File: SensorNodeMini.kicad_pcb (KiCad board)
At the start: 2 copper layers, 2 parts, among them U1 ArduinoProMini, U2 NRF24L01+

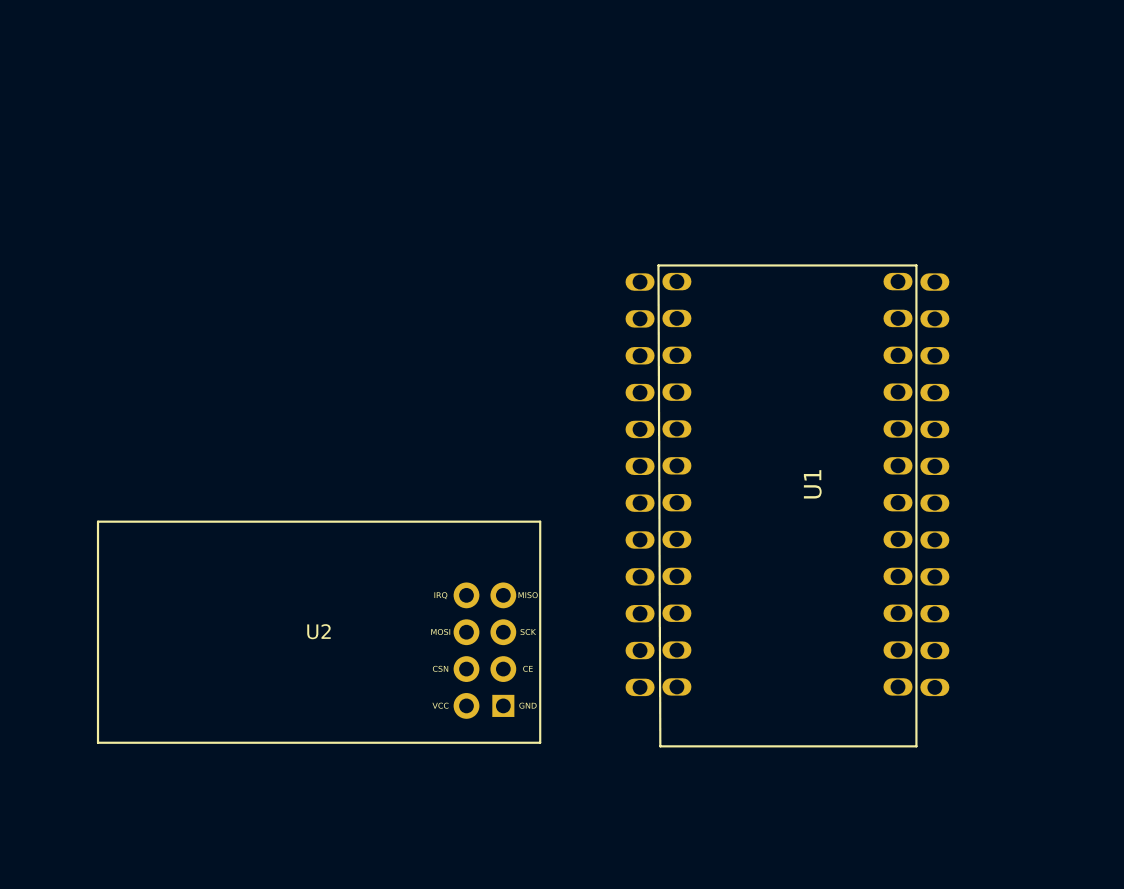
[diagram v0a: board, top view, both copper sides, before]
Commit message: added 3 mosfets, battery and connectors.
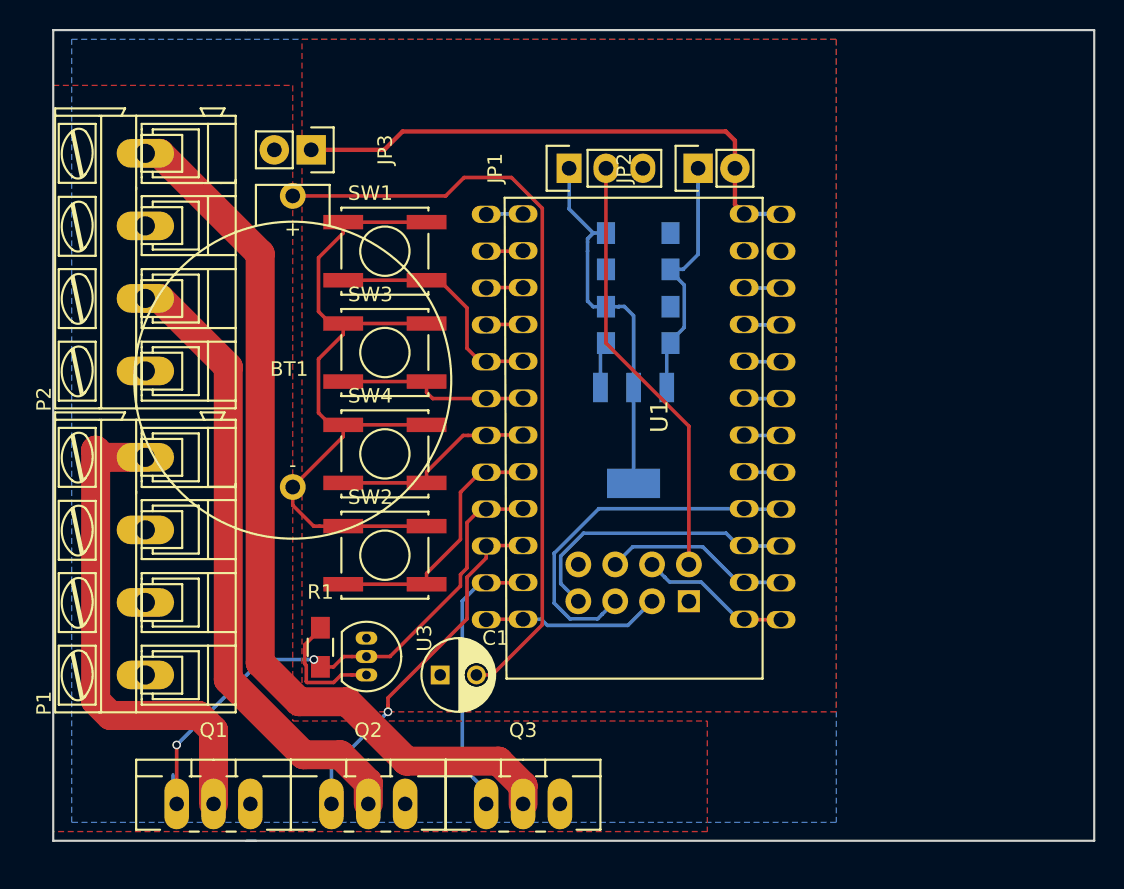
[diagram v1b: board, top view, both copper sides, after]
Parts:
- added BT1: Battery, MySensors:CR3032Holder, F.Cu at (139.1, 90.2)
- added C1: CP, Capacitors_ThroughHole:C_Radial_D5_L6_P2.5, F.Cu at (149.2, 110.5)
- added C2: 10u, Capacitors_SMD:C_0805_HandSoldering, B.Cu at (160.7, 86.4)
- added C3: 0.1u, Capacitors_SMD:C_0805_HandSoldering, B.Cu at (160.7, 81.3)
- added C4: 0.1u, Capacitors_SMD:C_0805_HandSoldering, B.Cu at (165.1, 86.4)
- added C5: 10u, Capacitors_SMD:C_0805_HandSoldering, B.Cu at (165.1, 81.3)
- added IC1: AMS1117, MySensors:SOT-223, B.Cu at (162.6, 94.0)
- added JP1: JUMPER3, Pin_Headers:Pin_Header_Straight_1x03, F.Cu at (158.1, 75.6)
- added JP2: JUMPER, Pin_Headers:Pin_Header_Straight_1x02, F.Cu at (167.0, 75.6)
- added JP3: JUMPER, Pin_Headers:Pin_Header_Straight_1x02, F.Cu at (140.3, 74.3)
- added P1: CONN_01X04, Connect:AK300-4, F.Cu at (128.9, 110.5)
- added P2: CONN_01X04, Connect:AK300-4, F.Cu at (128.9, 89.5)
- added Q1: Q_NMOS_GDS, TO_SOT_Packages_THT:TO-220_Neutral123_Vertical_LargePads, F.Cu at (133.6, 119.4)
- added Q2: Q_NMOS_GDS, TO_SOT_Packages_THT:TO-220_Neutral123_Vertical_LargePads, F.Cu at (144.3, 119.4)
- added Q3: Q_NMOS_GDS, TO_SOT_Packages_THT:TO-220_Neutral123_Vertical_LargePads, F.Cu at (154.9, 119.4)
- added R1: R, Resistors_SMD:R_0805_HandSoldering, F.Cu at (141.0, 108.6)
- added SW1: SW_PUSH, Buttons_Switches_SMD:SW_SPST_EVPBF, F.Cu at (145.4, 81.3)
- added SW2: SW_PUSH, Buttons_Switches_SMD:SW_SPST_EVPBF, F.Cu at (145.4, 102.2)
- added SW3: SW_PUSH, Buttons_Switches_SMD:SW_SPST_EVPBF, F.Cu at (145.4, 88.3)
- added SW4: SW_PUSH, Buttons_Switches_SMD:SW_SPST_EVPBF, F.Cu at (145.4, 95.2)
- added U3: DS18B20, TO_SOT_Packages_THT:TO-92_Inline_Narrow_Oval, F.Cu at (144.1, 108.0)
- U2: moved to B.Cu
- moved U1 11.6 mm to (162.6, 96.5)
- moved U2 11.3 mm to (158.8, 100.3), turned to 270 degrees
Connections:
- U1 pad 10: Net-(U1-Pad10) -> D7
- U1 pad 11: Net-(U1-Pad11) -> D8
- U1 pad 24: Net-(U1-Pad24) -> RAW
- U1 pad 9: Net-(U1-Pad9) -> D6
- U2 pad 8: VCC -> VCC_NRF
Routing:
- net VCC: track 0.00 -> 64.5 mm
- net Net-(P2-Pad4): track 0.00 -> 62.8 mm
- net GND: track 0.00 -> 55.2 mm
- net Net-(P2-Pad2): track 0.00 -> 44.2 mm
- net D6: track 0.00 -> 39.7 mm, vias 0 -> 2
- net RAW: track 0.00 -> 37.9 mm
- net Net-(P1-Pad4): track 0.00 -> 35.0 mm
- net VCC_NRF: track 0.00 -> 29.7 mm
- net Vout: track 0.00 -> 26.0 mm
- net SCK: track 0.00 -> 25.5 mm
- net D7: track 0.00 -> 24.8 mm, vias 0 -> 1
- net MISO: track 0.00 -> 19.8 mm
- net D8: track 0.00 -> 19.4 mm
- net Net-(SW2-Pad2): track 0.00 -> 18.0 mm
- net Net-(C4-Pad2): track 0.00 -> 17.3 mm
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- added copper zone on F.Cu, net +12V
- added copper zone on B.Cu, net GND
- added copper zone on F.Cu, net VCC
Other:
- board outline added: 71.8 x 55.9 mm
- net class +12v added: clearance 0.2, trace_width 2, via_dia 0.6, via_drill 0.4
- net class RAW added: clearance 0.2, trace_width 0.3, via_dia 0.6, via_drill 0.4

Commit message: routed everything, made gerbers.
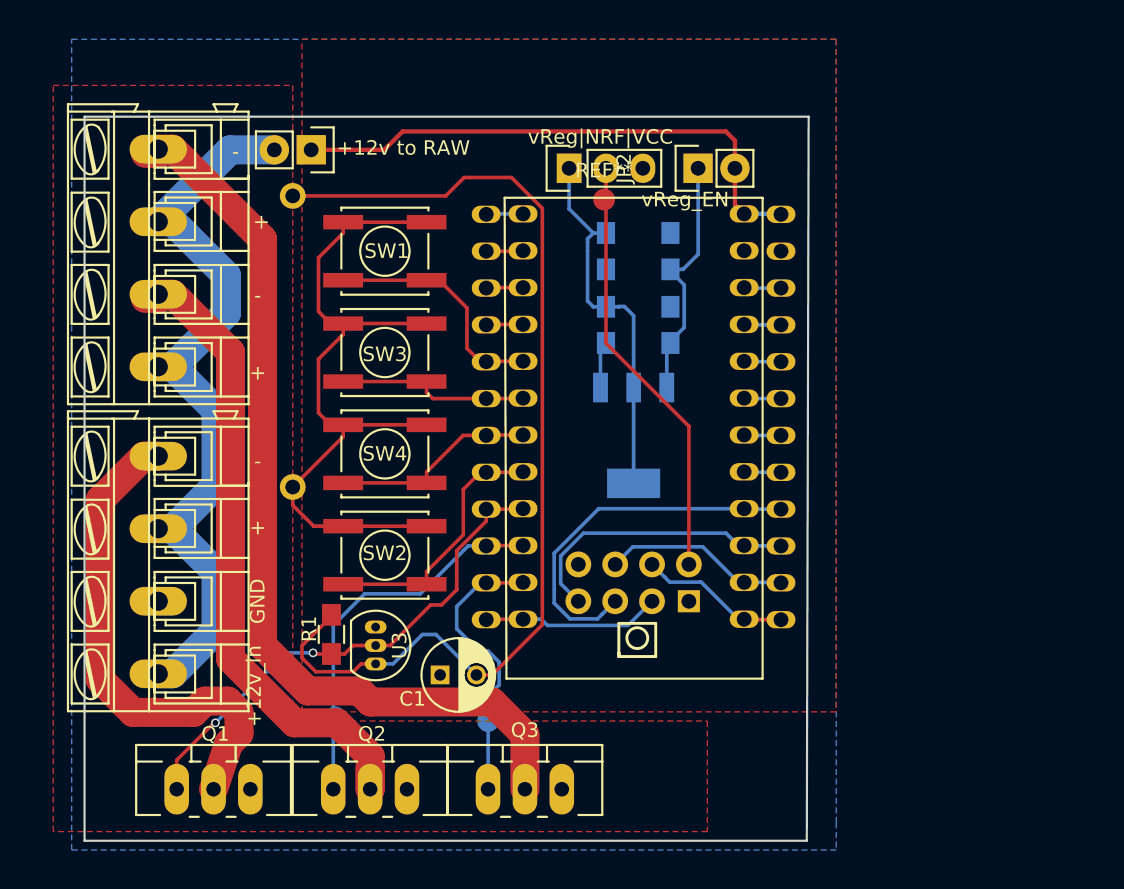
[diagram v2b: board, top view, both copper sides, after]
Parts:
- added REF**: Measurement_Point_Round-SMD-Pad_Small, Measurement_Points:Measurement_Point_Round-SMD-Pad_Small, F.Cu at (160.5, 77.7)
- added TP1: Measurement_Point_Round-SMD-Pad_Small, Measurement_Points:Measurement_Point_Round-SMD-Pad_Small, B.Cu at (137.8, 109.7)
- added TP2: Measurement_Point_Round-SMD-Pad_Small, Measurement_Points:Measurement_Point_Round-SMD-Pad_Small, B.Cu at (142.0, 113.4)
- added TP3: Measurement_Point_Round-SMD-Pad_Small, Measurement_Points:Measurement_Point_Round-SMD-Pad_Small, B.Cu at (152.5, 113.7)
- BT1: moved to B.Cu
- moved R1 1.17 mm to (141.7, 107.7)
- moved Q2 1.02 mm to (144.4, 118.4)
- moved Q3 1.02 mm to (155.1, 118.4)
- moved Q1 1.02 mm to (133.6, 118.4)
- moved U3 0.99 mm to (144.8, 107.2)
- moved P2 0.93 mm to (129.8, 89.2)
- moved P1 0.89 mm to (129.8, 110.4)
- turned BT1 to 180 degrees
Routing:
- net +12V: track 0.00 -> 53.2 mm
- net VCC: track 64.5 -> 74.3 mm
- net D6: track 39.7 -> 35.9 mm
- net D7: track 24.8 -> 28.1 mm, vias 1 -> 0
- net Net-(P2-Pad2): track 44.2 -> 45.8 mm
- net Net-(P2-Pad4): track 62.8 -> 64.1 mm
- net D8: track 19.4 -> 20.7 mm
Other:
- board size 71.8 x 55.9 mm -> 49.9 x 49.9 mm
- board text added: "+"
- board text added: "+12v to RAW"
- board text added: "+12v_in"
- board text added: "-"
- board text added: "GND"
- board text added: "vReg_EN"
- board text added: "vReg|NRF|VCC"

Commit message: v0.1, added microusb, removed some bugs, cleaned up the board
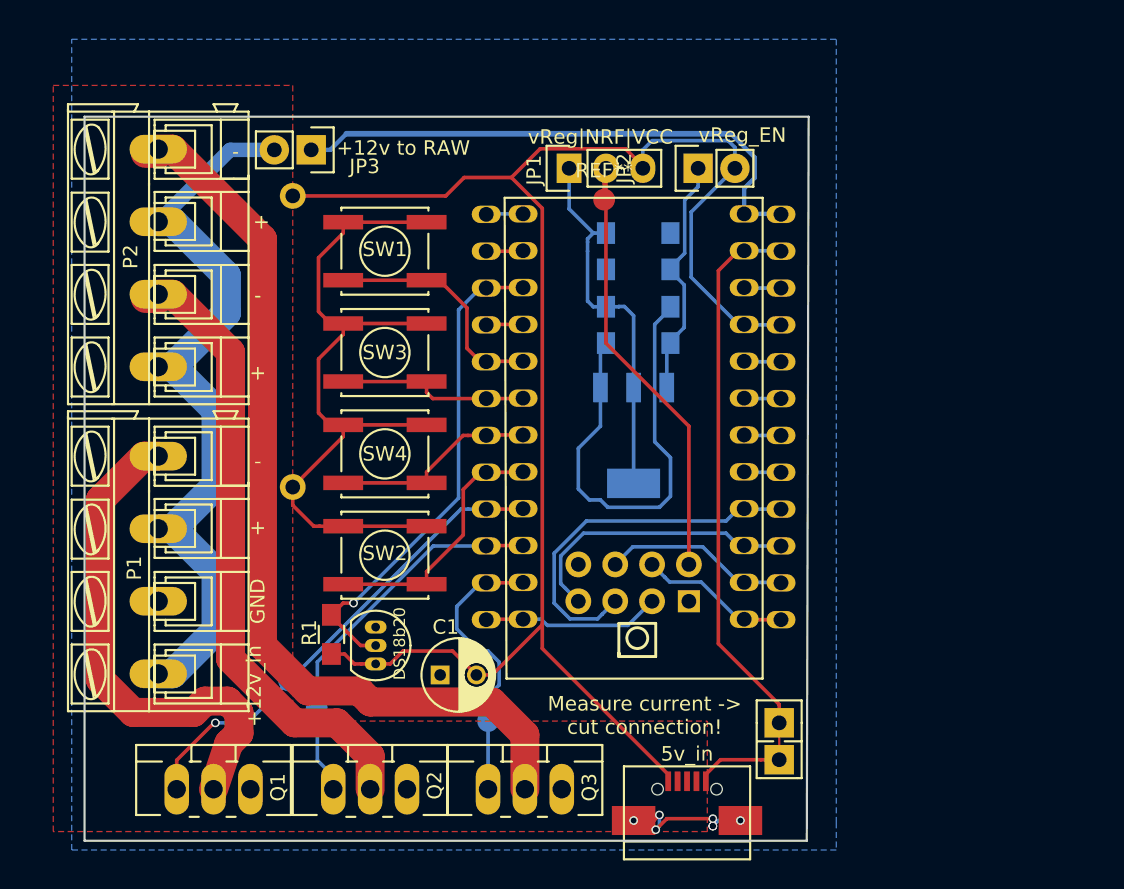
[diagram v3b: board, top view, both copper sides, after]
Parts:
- added 5v_in: USB_OTG, MySensors:USB_Micro-B_ebay, F.Cu at (166.2, 119.4)
- added JP4: Meas_cur, MySensors:Pin_Header_Straight_1x02_cuttable, F.Cu at (172.6, 113.8)
- JP1: value JUMPER3 -> NRF_3v3_SEL
- JP2: value JUMPER -> vReg_EN
- JP3: value JUMPER -> Feed_with_raw
- moved TP1 1.53 mm to (138.8, 110.9)
- moved TP2 1.42 mm to (140.7, 112.8)
- turned R1 to 270 degrees
- renumbered U1 to AMS1117_3v3, U3 to DS18b20
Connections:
- AMS1117_3v3 pad 23: GND -> Net-(JP4-Pad1)
- AMS1117_3v3 pad 3: Net-(U1-Pad3) -> D3
- DS18b20 pad 2: D6 -> D3
- JP2 pad 2: RAW -> VCC
- R1 pad 1: D6 -> D3
- REF** pad 1: (no net) -> VCC_NRF
- TP1 pad 1: (no net) -> D6
- TP2 pad 1: (no net) -> D7
- TP3 pad 1: (no net) -> D8
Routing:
- net VCC: track 74.3 -> 116.1 mm
- net Net-(JP4-Pad1): track 0.00 -> 37.8 mm
- net GND: track 55.2 -> 90.0 mm
- net D3: track 0.00 -> 34.2 mm, vias 0 -> 1
- net Net-(P3-Pad6): track 0.00 -> 9.88 mm, vias 0 -> 7
- net Net-(U1-Pad3): track 2.55 -> 0.00 mm
- net VCC_NRF: track 29.7 -> 31.9 mm
- net D6: track 35.9 -> 33.9 mm, vias 2 -> 1
- net Net-(P2-Pad2): track 45.8 -> 44.3 mm
- net D8: track 20.7 -> 21.8 mm
- net RAW: track 37.9 -> 38.5 mm
- net Net-(C4-Pad2): track 17.3 -> 16.8 mm
- removed copper zone on F.Cu, net VCC
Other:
- board text added: "Measure current -> cut connection!"
